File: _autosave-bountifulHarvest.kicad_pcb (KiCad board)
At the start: 2 copper layers, 159 parts, among them J10 CHECK FOOTPRINT, J11 Conn_01x02_Male, J12 CHECK FOOTPRINT, J13 CHECK FOOTPRINT, J14 Conn_01x02_Male, J15 Conn_01x02_Male, J6 CHECK FOOTPRINT, J7 CHECK FOOTPRINT, J8 Conn_01x02_Male, J9 Conn_01x02_Male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

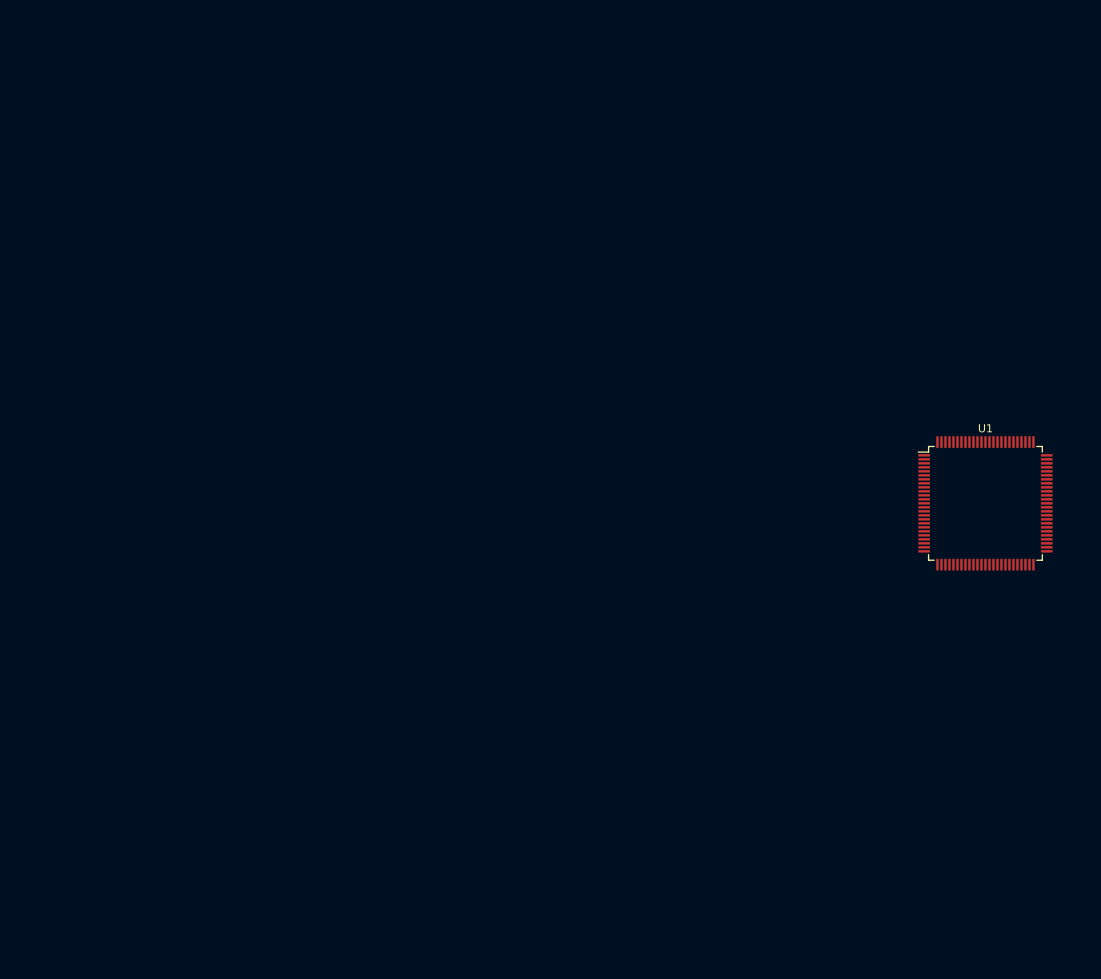
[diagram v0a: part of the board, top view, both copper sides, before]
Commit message: Updated bus connections between drivers at ATMega
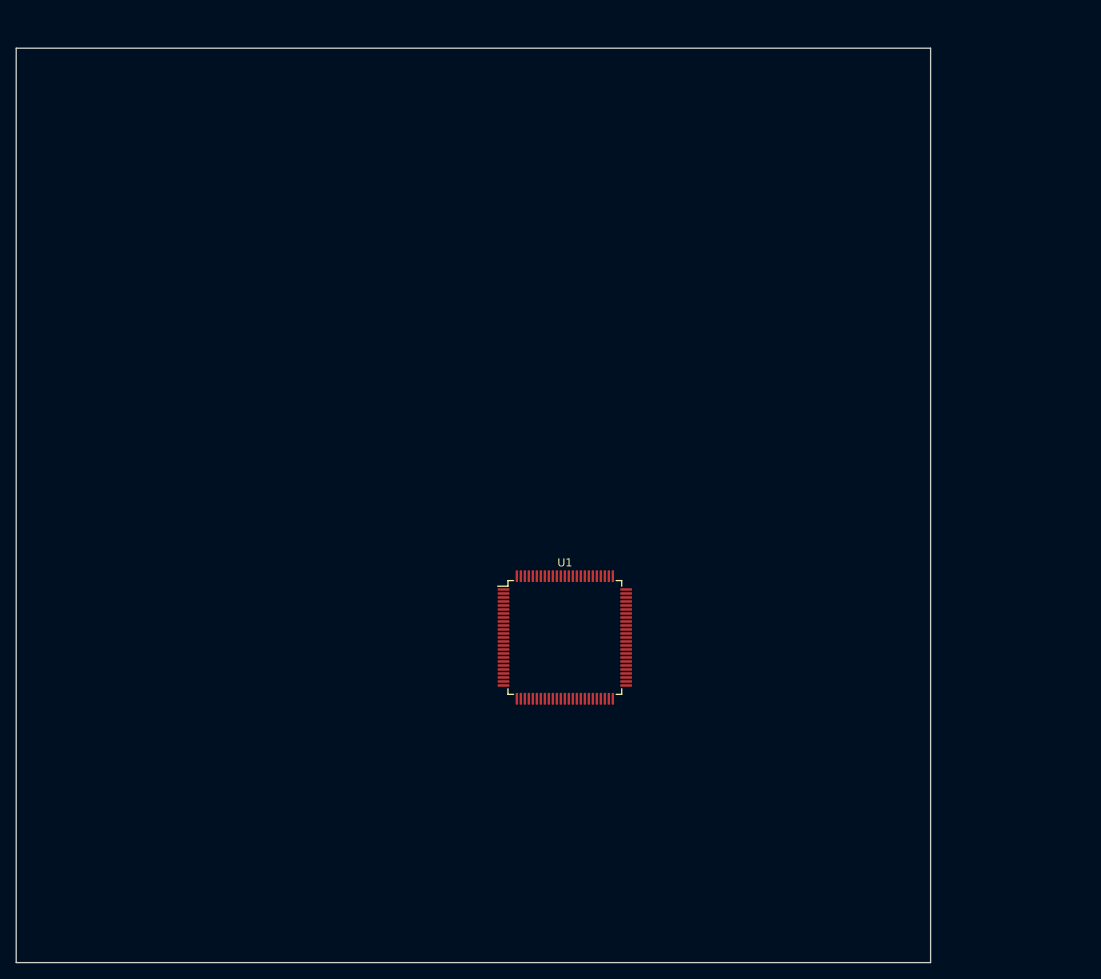
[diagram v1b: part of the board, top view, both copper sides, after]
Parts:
- moved U1 55.2 mm to (94.0, 99.1)
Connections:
- R42 pad 2: /Drivers/X_DIAG -> /Drivers/X_4
- TP3 pad 1: /Drivers/X_DIAG -> /Drivers/X_4
- U1 pad 43: (no net) -> /Drivers/X_0
- U1 pad 44: (no net) -> /Drivers/STEP_X
- U1 pad 45: (no net) -> /Drivers/DIR_X
- U1 pad 46: (no net) -> /Drivers/EN_X
- U1 pad 47: (no net) -> /Drivers/X_4
- U7 pad 2: (no net) -> /Drivers/X_0
- U7 pad 20: /Drivers/X_DIAG -> /Drivers/X_4
- U7 pad 21: /Drivers/X_DIAG -> /Drivers/X_4
- U7 pad 22: (no net) -> /Drivers/EN_X
- U7 pad 6: (no net) -> /Drivers/STEP_X
- U7 pad 7: (no net) -> /Drivers/DIR_X
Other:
- board outline added: 114.3 x 114.3 mm
